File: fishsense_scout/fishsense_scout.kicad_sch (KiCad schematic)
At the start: 0 parts

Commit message: Added footprint and buck converter schematic to KiCad
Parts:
- added U1: LMR16030PDDA, DDA0008E_N, symbol LMR16030:LMR16030PDDA
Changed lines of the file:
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@@
 	(generator_version "9.0")
 	(paper "A4")
+	(symbol
+		(lib_id "LMR16030:LMR16030PDDA")
+		(at 143.51 99.06 0)
+		(unit 1)
+		(exclude_from_sim no)
+		(in_bom yes)
+		(on_board yes)
+		(dnp no)
+		(fields_autoplaced yes)
+		(property "Reference" "U1"
+			(at 143.51 78.74 0)
+			(effects
+				(font
+					(size 1.524 1.524)
+				)
+			)
+		)
+		(property "Value" "LMR16030PDDA"
+			(at 143.51 81.28 0)
+			(effects
+				(font
+					(size 1.524 1.524)
+				)
+			)
+		)
+		(property "Footprint" "DDA0008E_N"
+			(at 143.51 99.06 0)
+			(effects
+				(font
+					(size 1.27 1.27)
+					(italic yes)
+				)
+				(hide yes)
+			)
+		)
+		(property "Datasheet" "https://www.ti.com/lit/gpn/lmr16030"
+			(at 143.51 99.06 0)
+			(effects
+				(font
+					(size 1.27 1.27)
+					(italic yes)
+				)
+				(hide yes)
+			)
+		)
+		(property "Description" ""
+			(at 143.51 99.06 0)
+			(effects
+				(font
+					(size 1.27 1.27)
+				)
+				(hide yes)
+			)
+		)
+		(pin "2"
+		)
+		(pin "4"
+		)
+		(pin "6"
+		)
+		(pin "3"
+		)
+		(pin "8"
+		)
+		(pin "1"
+		)
+		(pin "5"
+		)
+		(pin "7"
+		)
+		(pin "9"
+		)
+		(instances
+			(project ""
+				(path "/b26a8f70-3022-4080-8df6-954fec2d4ddd"
+					(reference "U1")
+					(unit 1)
+				)
+			)
+		)
+	)
 	(sheet_instances
 		(path "/"

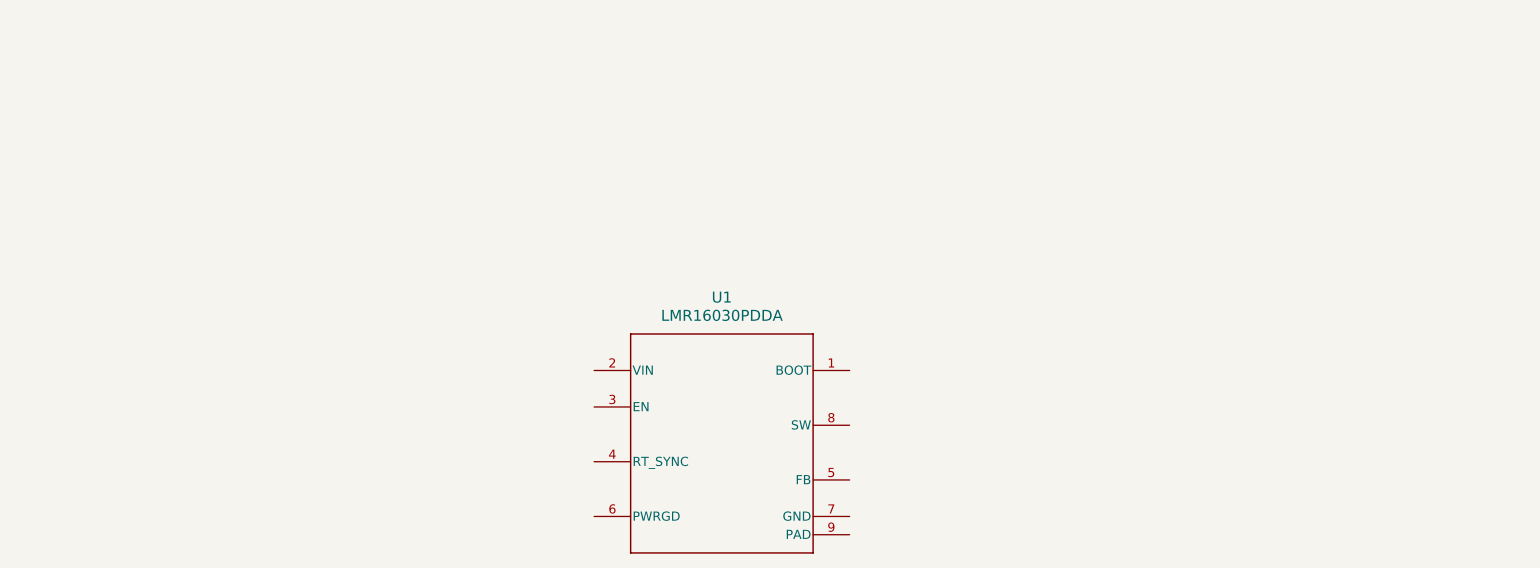
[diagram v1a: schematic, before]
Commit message: Finished PCB schematic design along with ERC check, assigned footprints, and made rough arrangement of components in PCB
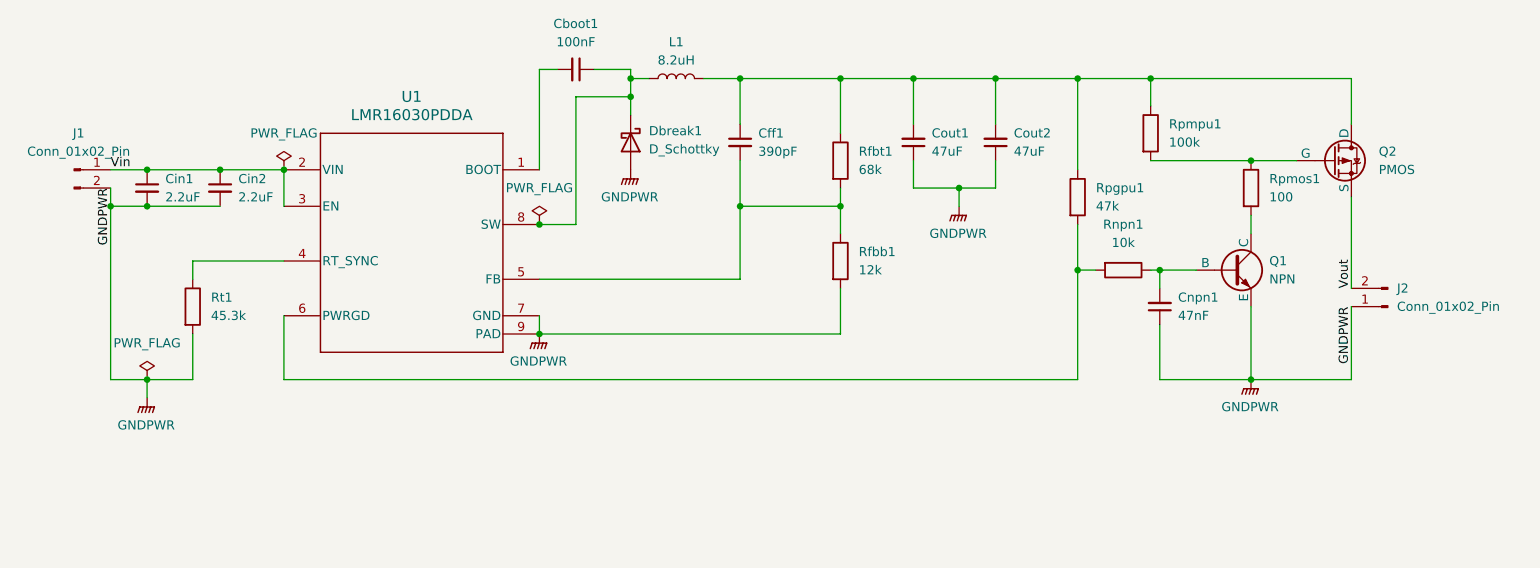
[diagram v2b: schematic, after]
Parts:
- added Cboot1: 100nF, Capacitor_SMD:C_0603_1608Metric, symbol Device:C_Small
- added Cff1: 390pF, Capacitor_SMD:C_0603_1608Metric, symbol Device:C_Small
- added Cin1, Cin2: 2.2uF, Capacitor_SMD:C_1210_3225Metric, symbol Device:C_Small
- added Cnpn1: 47nF, Capacitor_SMD:C_0603_1608Metric, symbol Device:C_Small
- added Cout1, Cout2: 47uF, Capacitor_SMD:C_1210_3225Metric, symbol Device:C_Small
- added Dbreak1: D_Schottky, Diode_SMD:D_SMB, symbol Device:D_Schottky
- added J1, J2: Conn_01x02_Pin, Connector_PinSocket_2.54mm:PinSocket_1x02_P2.54mm_Vertical, symbol Connector:Conn_01x02_Pin
- added L1: 8.2uH, Inductor_SMD:L_7.3x7.3_H3.5, symbol Device:L
- added Q1: NPN, Package_TO_SOT_SMD:SOT-23, symbol Simulation_SPICE:NPN
- added Q2: PMOS, Package_TO_SOT_SMD:SOT-23, symbol Simulation_SPICE:PMOS
- added Rfbb1: 12k, Resistor_SMD:R_0603_1608Metric, symbol Device:R
- added Rfbt1: 68k, Resistor_SMD:R_0603_1608Metric, symbol Device:R
- added Rnpn1: 10k, Resistor_SMD:R_0603_1608Metric, symbol Device:R
- added Rpgpu1: 47k, Resistor_SMD:R_0603_1608Metric, symbol Device:R
- added Rpmos1: 100, Resistor_SMD:R_0603_1608Metric, symbol Device:R
- added Rpmpu1: 100k, Resistor_SMD:R_0603_1608Metric, symbol Device:R
- added Rt1: 45.3k, Resistor_SMD:R_0603_1608Metric, symbol Device:R
- U1: footprint DDA0008E_N -> Package_SO:SOIC-8-1EP_3.9x4.9mm_P1.27mm_EP2.514x3.2mm_ThermalVias
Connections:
- net at U1.1 (BOOT): now also Cboot1.2
- net Vin: now reaches U1.2 (VIN)
- net Vin: now also U1.3 (EN), Cin1.1, Cin2.1, J1.1 (Pin_1)
- net at U1.4 (RT_SYNC): now also Rt1.1
- net at U1.5 (FB): now also Cff1.2, Rfbb1.1, Rfbt1.2
- net at U1.6 (PWRGD): now also Rnpn1.2, Rpgpu1.2
- net GNDPWR: now reaches U1.7 (GND)
- net GNDPWR: now also U1.9 (PAD), Cin1.2, Cin2.2, Cnpn1.1, Cout1.1, Cout2.1, Dbreak1.2 (A), J1.2 (Pin_2), J2.1 (Pin_1), Q1.3 (E), Rfbb1.2, Rt1.2
- net at U1.8 (SW): now also Cboot1.1, Dbreak1.1 (K), L1.1
- new net: Cff1.1, Cout1.2, Cout2.2, L1.2, Q2.1 (D), Rfbt1.1, Rpgpu1.1, Rpmpu1.1
- new net: Q2.2 (G), Rpmos1.1, Rpmpu1.2
- new net: Cnpn1.2, Q1.2 (B), Rnpn1.1
- new net: Q1.1 (C), Rpmos1.2
- new net Vout: J2.2 (Pin_2), Q2.3 (S)
